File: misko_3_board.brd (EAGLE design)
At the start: 96 x 162 mm, 179 parts, among them IC1 ATMEGA1281-16AU, IC10 ORG1510-MK4, IC11 TPS3808G33DBVT, IC12 LTC4425, IC13 RN-42, IC14 ADXL345, IC15 74HCT1G32, IC16 FM25W256-SOIC, IC17 MICROSD_SPI_MODE, IC18 FH12-30S-0.5SH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

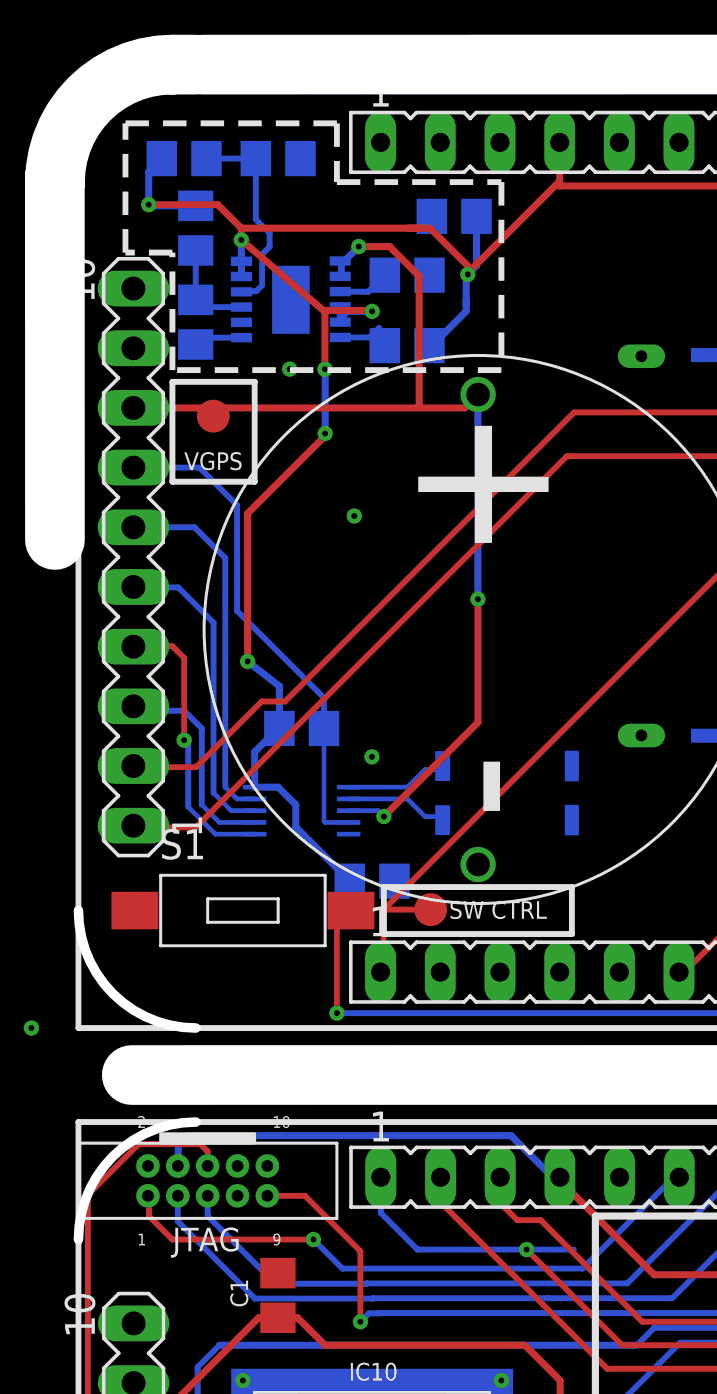
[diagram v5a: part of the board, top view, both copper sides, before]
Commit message: - corrected resisitor divider for LTC4425 - R60/61 now connect to Vgps (instead of Vcc)
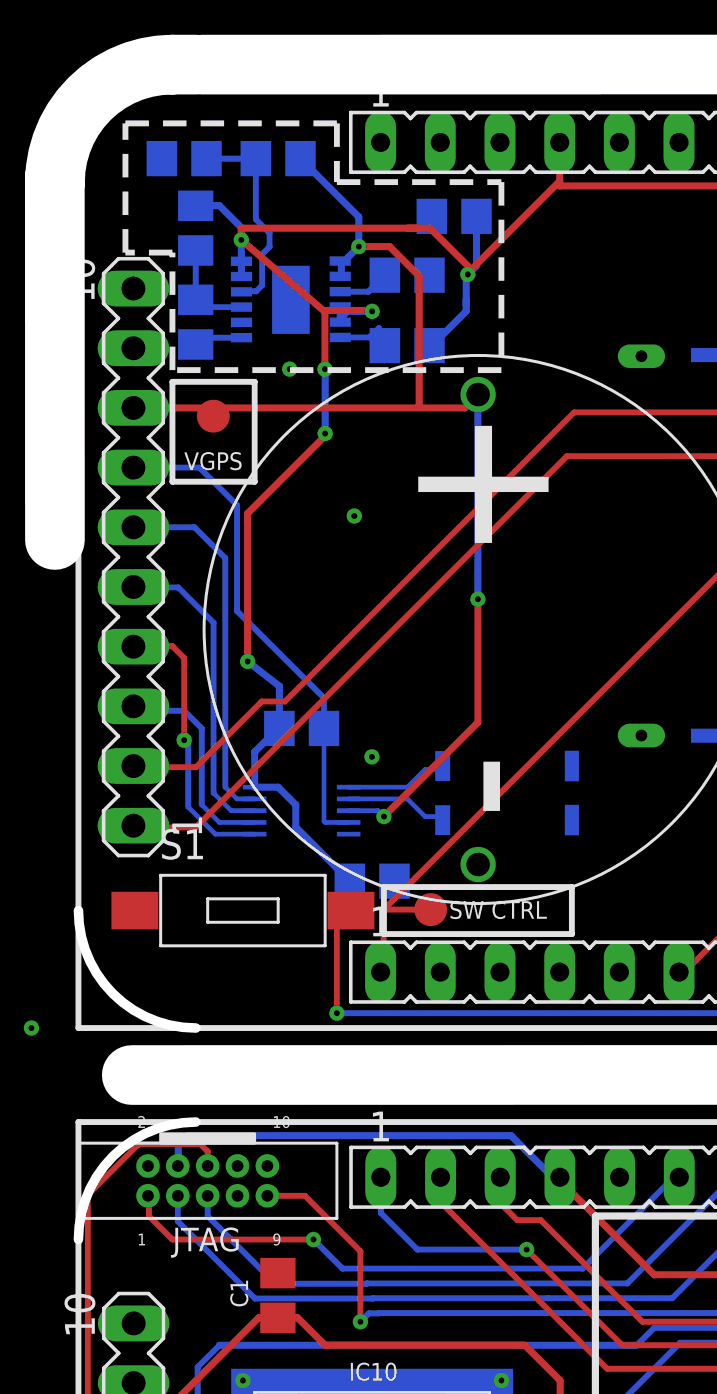
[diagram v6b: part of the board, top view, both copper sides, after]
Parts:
- moved R60 4.00 mm to (8.50, 125.0), turned to 180 degrees
- moved R61 4.00 mm to (4.50, 125.0), turned to 180 degrees
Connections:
- net VCC: no longer R60.2
- net VGPS: now also R60.2
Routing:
- net VCC: track 459.8 -> 454.1 mm, vias 34 -> 33
- net VGPS: track 107.3 -> 112.0 mm
- net RXD: track 64.5 -> 62.5 mm
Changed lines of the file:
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@@
 <setting verticaltext="up"/>
 </settings>
-<grid distance="1" unitdist="mm" unit="mm" style="lines" multiple="1" display="yes" altdistance="0.005" altunitdist="mm" altunit="mm"/>
+<grid distance="0.5" unitdist="mm" unit="mm" style="lines" multiple="1" display="yes" altdistance="0.005" altunitdist="mm" altunit="mm"/>
 <layers>
 <layer number="1" name="Top" color="4" fill="1" visible="yes" active="yes"/>
@@
 <attribute name="SPICETYPE" value="diode" x="97" y="10" size="1.778" layer="27" rot="R180" display="off"/>
 </element>
-<element name="R60" library="resistor" package="R0805" value="470k" x="4.5" y="125" rot="MR0"/>
-<element name="R61" library="resistor" package="R0805" value="470k" x="8.5" y="125" rot="MR0"/>
+<element name="R60" library="resistor" package="R0805" value="470k" x="8.5" y="125" rot="MR180"/>
+<element name="R61" library="resistor" package="R0805" value="470k" x="4.5" y="125" rot="MR180"/>
 <element name="S1" library="DTSM-32N-B" package="DTSM-32N-B" value="" x="7" y="93">
 <attribute name="MF" value="" x="7" y="93" size="1.778" layer="27" display="off"/>
@@
 <via x="34.2212" y="10.74" extent="1-16" drill="0.7" shape="octagon"/>
 <contactref element="IC20" pad="VCC"/>
-<wire x1="5.04" y1="123.04" x2="4.99" y2="122.99" width="0.3" layer="16"/>
+<wire x1="4.99" y1="122.99" x2="5.04" y2="123.04" width="0.3" layer="16"/>
 <wire x1="16.57" y1="120.07" x2="16.54" y2="120.04" width="0.3" layer="16"/>
 <via x="16.57" y="120.07" extent="1-16" drill="0.25"/>
@@
 <wire x1="34.99" y1="107.3354" x2="34.99" y2="106.64520625" width="0.3" layer="1"/>
 <wire x1="34.99" y1="106.64520625" x2="34.53919375" y2="106.1944" width="0.3" layer="1"/>
-<wire x1="4.99" y1="122.99" x2="3.04" y2="122.99" width="0.3" layer="16"/>
-<wire x1="3.04" y1="122.99" x2="2.99" y2="123.04" width="0.3" layer="16"/>
-<via x="2.99" y="123.04" extent="1-16" drill="0.25"/>
-<wire x1="5.9308" y1="123.04" x2="2.99" y2="123.04" width="0.3" layer="1"/>
 <via x="6.9308" y="121.54" extent="1-16" drill="0.25"/>
 <wire x1="10.49" y1="116.04" x2="10.39" y2="116.14" width="0.3" layer="16"/>
@@
 <wire x1="67.25" y1="50.25" x2="72.584" y2="55.584" width="0.3" layer="1"/>
 <wire x1="6.94" y1="120.63" x2="6.94" y2="120.94" width="0.3" layer="16"/>
-<wire x1="6.9308" y1="121.54" x2="6.9308" y2="120.6392" width="0.3" layer="16"/>
+<wire x1="6.9308" y1="120.6392" x2="6.9308" y2="121.54" width="0.3" layer="16"/>
 <wire x1="6.9308" y1="120.6392" x2="6.94" y2="120.63" width="0.3" layer="16"/>
 <wire x1="6.9308" y1="121.54" x2="6.9308" y2="122.04" width="0.3" layer="1"/>
-<wire x1="6.9308" y1="122.04" x2="5.9308" y2="123.04" width="0.3" layer="1"/>
 <wire x1="14.96" y1="122.04" x2="6.9308" y2="122.04" width="0.3" layer="1"/>
 <wire x1="14" y1="122.04" x2="14.46" y2="122.04" width="0.3" layer="1"/>
@@
 <wire x1="12.5" y1="118.5" x2="11.33" y2="118.5" width="0.3" layer="16"/>
 <wire x1="11.33" y1="118.5" x2="11.14" y2="118.69" width="0.3" layer="16"/>
-<contactref element="R60" pad="2"/>
-<wire x1="2.99" y1="123.04" x2="2.99" y2="124.44" width="0.3" layer="16"/>
-<wire x1="2.99" y1="124.44" x2="3.55" y2="125" width="0.3" layer="16"/>
+<wire x1="6.9308" y1="121.54" x2="6.9308" y2="122.0692" width="0.3" layer="16"/>
+<wire x1="6.9308" y1="122.0692" x2="6" y2="123" width="0.3" layer="16"/>
+<wire x1="6" y1="123" x2="5" y2="123" width="0.3" layer="16"/>
+<wire x1="5" y1="123" x2="4.99" y2="122.99" width="0.3" layer="16"/>
 <wire x1="20.48" y1="125.69" x2="15.37" y2="145" width="0" layer="19" extent="1-1"/>
 <wire x1="16.5" y1="119" x2="16.5" y2="118.75" width="0" layer="19" extent="16-16"/>
@@
 <wire x1="13.245" y1="121.255" x2="14.5" y2="120" width="0.3" layer="1"/>
 <wire x1="14.5" y1="120" x2="14.5" y2="114.5" width="0.3" layer="1"/>
+<contactref element="R60" pad="2"/>
+<wire x1="11.9308" y1="121.255" x2="11.9308" y2="122.5192" width="0.3" layer="16"/>
+<wire x1="11.9308" y1="122.5192" x2="9.45" y2="125" width="0.3" layer="16"/>
 <wire x1="16.44" y1="114.39" x2="14.5" y2="114.5" width="0" layer="19" extent="1-1"/>
 <wire x1="17" y1="115.03" x2="17.01" y2="114.96" width="0" layer="19" extent="16-16"/>
@@
 <contactref element="R60" pad="1"/>
 <contactref element="R61" pad="2"/>
+<wire x1="7.55" y1="122.415275" x2="8.134" y2="121.831275" width="0.25" layer="16"/>
 <wire x1="5.45" y1="125" x2="7.55" y2="125" width="0.25" layer="16"/>
 <wire x1="7.55" y1="125" x2="7.55" y2="122.415275" width="0.25" layer="16"/>
-<wire x1="7.55" y1="122.415275" x2="8.134" y2="121.831275" width="0.25" layer="16"/>
 </signal>
 <signal name="PFI_RET" class="2">
@@
 <wire x1="12.87" y1="81.65" x2="12.87" y2="80.13" width="0.25" layer="16"/>
 <wire x1="23.1443875" y1="74.5" x2="19.07219375" y2="78.57219375" width="0.25" layer="1"/>
-<wire x1="21.07" y1="78.56" x2="21.07" y2="78.57" width="0.25" layer="16"/>
-<wire x1="21.07" y1="78.57" x2="19.07219375" y2="78.57219375" width="0.25" layer="16"/>
 <via x="19.07219375" y="78.57219375" extent="1-16" drill="0.25"/>
 <wire x1="19.07219375" y1="78.57219375" x2="14.42780625" y2="78.57219375" width="0.25" layer="16"/>

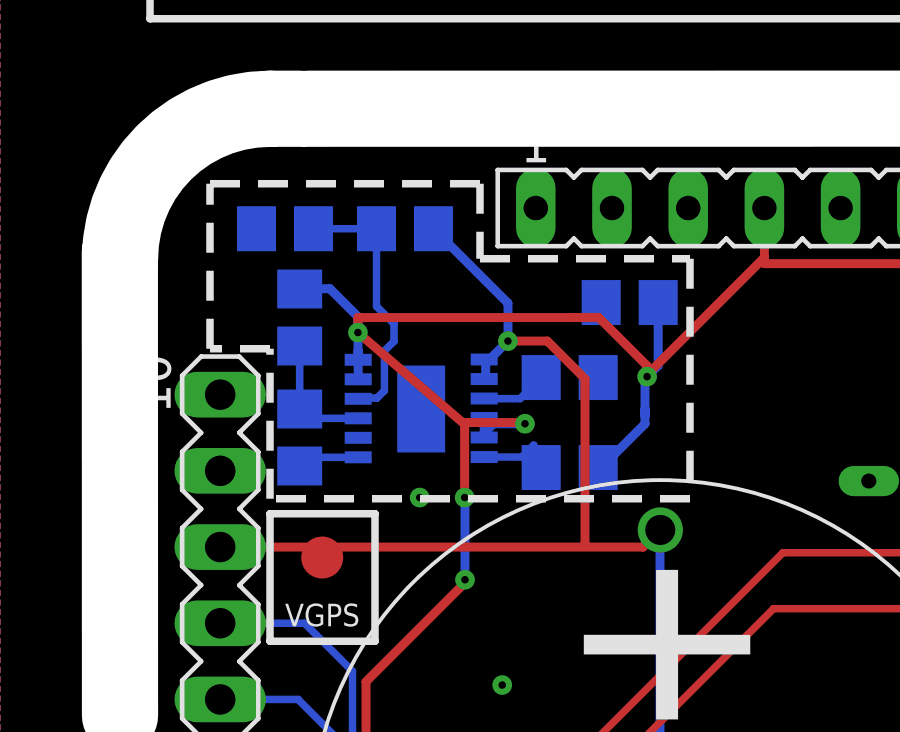
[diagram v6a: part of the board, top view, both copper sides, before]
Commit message: - removed power fail functionality from LTC4425 since it is not needed at all
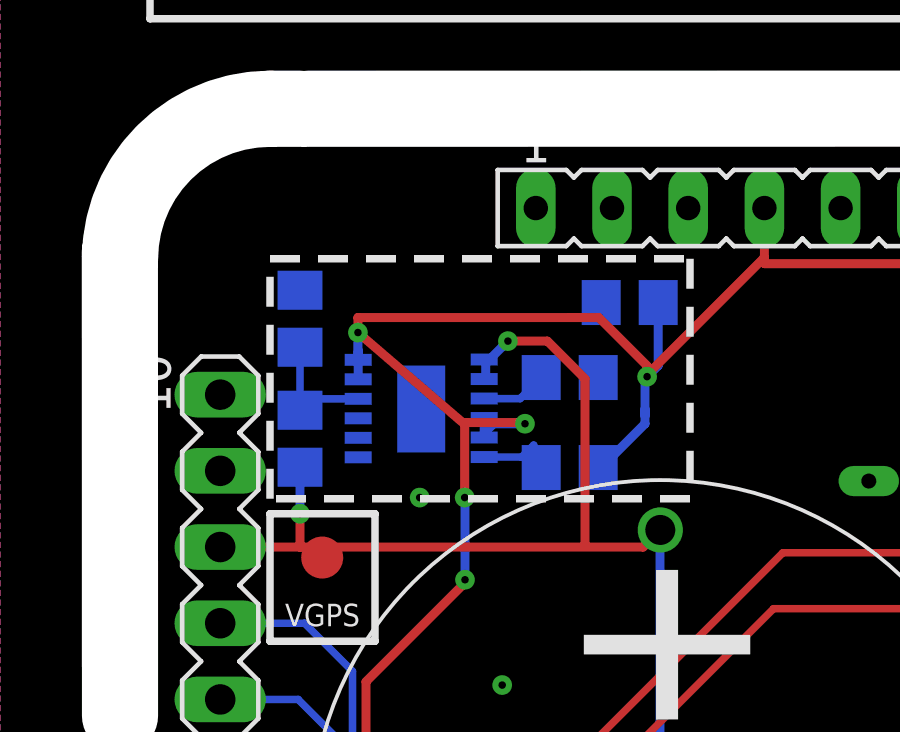
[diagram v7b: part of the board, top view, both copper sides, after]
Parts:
- removed R37, R38: 150k, resistor:R0805
- moved R60 7.83 mm to (5.00, 118.0), turned to 270 degrees
- moved R61 3.04 mm to (5.00, 122.0), turned to 270 degrees
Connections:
- removed net PFI: IC12.PFI, R37.2, R38.1
- net PFI_RET: no longer R37.1
- net VCC: no longer R38.2
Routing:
- net VMID: track 9.00 -> 4.33 mm
- net PFI: track 4.18 -> 0.00 mm
- net VCC: track 454.1 -> 451.2 mm
- net VGPS: track 112.0 -> 109.9 mm, vias 5 -> 6
- net PFI_RET: track 2.07 -> 0.00 mm
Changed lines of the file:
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@@
 <wire x1="18" y1="124" x2="18" y2="116" width="0.25" layer="21" style="shortdash"/>
 <wire x1="18" y1="116" x2="4" y2="116" width="0.25" layer="21" style="shortdash"/>
-<wire x1="4" y1="116" x2="4" y2="121" width="0.25" layer="21" style="shortdash"/>
-<wire x1="4" y1="121" x2="2" y2="121" width="0.25" layer="21" style="shortdash"/>
-<wire x1="2" y1="121" x2="2" y2="126.5" width="0.25" layer="21" style="shortdash"/>
-<wire x1="2" y1="126.5" x2="11" y2="126.5" width="0.25" layer="21" style="shortdash"/>
-<wire x1="11" y1="126.5" x2="11" y2="124" width="0.25" layer="21" style="shortdash"/>
-<wire x1="11" y1="124" x2="18" y2="124" width="0.25" layer="21" style="shortdash"/>
-<wire x1="17.99" y1="124.04" x2="10.99" y2="124.04" width="0.25" layer="22" style="shortdash"/>
-<wire x1="10.99" y1="124.04" x2="10.99" y2="126.54" width="0.254" layer="22" style="shortdash"/>
-<wire x1="10.99" y1="126.54" x2="1.99" y2="126.54" width="0.25" layer="22" style="shortdash"/>
-<wire x1="1.99" y1="126.54" x2="1.99" y2="121.04" width="0.25" layer="22" style="shortdash"/>
-<wire x1="1.99" y1="121.04" x2="3.99" y2="121.04" width="0.25" layer="22" style="shortdash"/>
-<wire x1="3.99" y1="121.04" x2="3.99" y2="116.04" width="0.25" layer="22" style="shortdash"/>
+<wire x1="4" y1="116" x2="4" y2="124" width="0.25" layer="21" style="shortdash"/>
+<wire x1="4" y1="124" x2="18" y2="124" width="0.25" layer="21" style="shortdash"/>
+<wire x1="17.99" y1="124.04" x2="3.99" y2="124.04" width="0.25" layer="22" style="shortdash"/>
+<wire x1="3.99" y1="124.04" x2="3.99" y2="116.04" width="0.25" layer="22" style="shortdash"/>
 <wire x1="3.99" y1="116.04" x2="17.99" y2="116.04" width="0.25" layer="22" style="shortdash"/>
 <wire x1="17.99" y1="116.04" x2="17.99" y2="124.04" width="0.25" layer="22" style="shortdash"/>
@@
 <attribute name="VALUE" x="21.865" y="67.54" size="1.27" layer="28" rot="MR180"/>
 </element>
-<element name="R37" library="resistor" package="R0805" value="150k" x="4.99" y="118.04" smashed="yes" rot="MR90">
-<attribute name="NAME" x="6.25" y="117" size="0.75" layer="26" rot="MR90"/>
-<attribute name="VALUE" x="2.45" y="117.405" size="1.27" layer="28" rot="MR90"/>
-</element>
-<element name="R38" library="resistor" package="R0805" value="150k" x="4.99" y="122.04" smashed="yes" rot="MR90">
-<attribute name="NAME" x="6.25" y="121.25" size="0.75" layer="26" rot="MR90"/>
-<attribute name="VALUE" x="2.45" y="121.405" size="1.27" layer="28" rot="MR90"/>
-</element>
 <element name="R39" library="resistor" package="R0805" value="1k" x="13.99" y="117.04" smashed="yes" rot="MR0">
 <attribute name="NAME" x="17.75" y="116.5" size="0.75" layer="26" rot="MR0"/>
@@
 <attribute name="SPICETYPE" value="diode" x="97" y="10" size="1.778" layer="27" rot="R180" display="off"/>
 </element>
-<element name="R60" library="resistor" package="R0805" value="470k" x="8.5" y="125" rot="MR180"/>
-<element name="R61" library="resistor" package="R0805" value="470k" x="4.5" y="125" rot="MR180"/>
+<element name="R60" library="resistor" package="R0805" value="470k" x="5" y="118" rot="MR270"/>
+<element name="R61" library="resistor" package="R0805" value="470k" x="5" y="122" rot="MR270"/>
 <element name="S1" library="DTSM-32N-B" package="DTSM-32N-B" value="" x="7" y="93">
 <attribute name="MF" value="" x="7" y="93" size="1.778" layer="27" display="off"/>
@@
 <contactref element="IC12" pad="FB"/>
 <contactref element="IC12" pad="SEL"/>
-<contactref element="R38" pad="2"/>
 <contactref element="IC12" pad="VIN1"/>
 <contactref element="C21" pad="2"/>
@@
 <via x="34.2212" y="10.74" extent="1-16" drill="0.7" shape="octagon"/>
 <contactref element="IC20" pad="VCC"/>
-<wire x1="4.99" y1="122.99" x2="5.04" y2="123.04" width="0.3" layer="16"/>
 <wire x1="16.57" y1="120.07" x2="16.54" y2="120.04" width="0.3" layer="16"/>
 <via x="16.57" y="120.07" extent="1-16" drill="0.25"/>
@@
 <wire x1="12.5" y1="118.5" x2="11.33" y2="118.5" width="0.3" layer="16"/>
 <wire x1="11.33" y1="118.5" x2="11.14" y2="118.69" width="0.3" layer="16"/>
-<wire x1="6.9308" y1="121.54" x2="6.9308" y2="122.0692" width="0.3" layer="16"/>
-<wire x1="6.9308" y1="122.0692" x2="6" y2="123" width="0.3" layer="16"/>
-<wire x1="6" y1="123" x2="5" y2="123" width="0.3" layer="16"/>
-<wire x1="5" y1="123" x2="4.99" y2="122.99" width="0.3" layer="16"/>
 <wire x1="20.48" y1="125.69" x2="15.37" y2="145" width="0" layer="19" extent="1-1"/>
 <wire x1="16.5" y1="119" x2="16.5" y2="118.75" width="0" layer="19" extent="16-16"/>
@@
 <wire x1="5" y1="28" x2="6.05" y2="28" width="0.3048" layer="1"/>
 <wire x1="5.49" y1="114.39" x2="16.44" y2="114.39" width="0.3" layer="1"/>
-<wire x1="5.49" y1="114.39" x2="2.34" y2="114.39" width="0.3" layer="1"/>
+<wire x1="5.49" y1="114.39" x2="5" y2="114.39" width="0.3" layer="1"/>
 <contactref element="TP10" pad="TP"/>
+<wire x1="5" y1="114.39" x2="2.34" y2="114.39" width="0.3" layer="1"/>
 <wire x1="5.74" y1="114.04" x2="5.49" y2="114.39" width="0.3" layer="1"/>
 <contactref element="TP11" pad="TP"/>
@@
 <wire x1="14.5" y1="120" x2="14.5" y2="114.5" width="0.3" layer="1"/>
 <contactref element="R60" pad="2"/>
-<wire x1="11.9308" y1="121.255" x2="11.9308" y2="122.5192" width="0.3" layer="16"/>
-<wire x1="11.9308" y1="122.5192" x2="9.45" y2="125" width="0.3" layer="16"/>
+<wire x1="11.9308" y1="121.255" x2="11.9308" y2="122.5192" width="0" layer="19" extent="1-16"/>
+<wire x1="5" y1="114.39" x2="5" y2="115.5" width="0.3" layer="1"/>
+<via x="5" y="115.5" extent="1-16" drill="0.25"/>
+<wire x1="5" y1="115.5" x2="5" y2="117.05" width="0.3" layer="16"/>
 <wire x1="16.44" y1="114.39" x2="14.5" y2="114.5" width="0" layer="19" extent="1-1"/>
 <wire x1="17" y1="115.03" x2="17.01" y2="114.96" width="0" layer="19" extent="16-16"/>
@@
 <wire x1="6.05" y1="28" x2="14.5" y2="55" width="0" layer="19" extent="1-1"/>
 </signal>
-<signal name="PFI" class="2">
-<contactref element="R37" pad="2"/>
-<contactref element="R38" pad="1"/>
-<contactref element="IC12" pad="PFI"/>
-<wire x1="4.99" y1="118.99" x2="4.99" y2="121.09" width="0.254" layer="16"/>
-<wire x1="6.94" y1="118.68" x2="5.3" y2="118.68" width="0.25" layer="16"/>
-<wire x1="5.3" y1="118.68" x2="4.99" y2="118.99" width="0.25" layer="16"/>
-</signal>
 <signal name="LTC4425_PROG" class="2">
 <contactref element="R40" pad="2"/>
@@
 <contactref element="IC12" pad="VMID"/>
 <wire x1="6.80841875" y1="119.29" x2="6.94" y2="119.33" width="0.254" layer="16"/>
-<wire x1="7.56604375" y1="119.355" x2="7.815" y2="119.60395625" width="0.25" layer="16"/>
-<wire x1="7.815" y1="120.929725" x2="8.134" y2="121.248725" width="0.25" layer="16"/>
-<wire x1="8.134" y1="121.831275" x2="8.134" y2="121.248725" width="0.25" layer="16"/>
-<wire x1="7.815" y1="119.60395625" x2="7.815" y2="120.929725" width="0.25" layer="16"/>
-<wire x1="6.94" y1="119.33" x2="6.965" y2="119.355" width="0.25" layer="16"/>
-<wire x1="6.965" y1="119.355" x2="7.56604375" y2="119.355" width="0.25" layer="16"/>
 <contactref element="R60" pad="1"/>
 <contactref element="R61" pad="2"/>
-<wire x1="7.55" y1="122.415275" x2="8.134" y2="121.831275" width="0.25" layer="16"/>
-<wire x1="5.45" y1="125" x2="7.55" y2="125" width="0.25" layer="16"/>
-<wire x1="7.55" y1="125" x2="7.55" y2="122.415275" width="0.25" layer="16"/>
-</signal>
-<signal name="PFI_RET" class="2">
-<contactref element="R37" pad="1"/>
-<contactref element="IC12" pad="PFI_RET"/>
-<wire x1="6.94" y1="117.38" x2="5.28" y2="117.38" width="0.25" layer="16"/>
-<wire x1="5.28" y1="117.38" x2="4.99" y2="117.09" width="0.25" layer="16"/>
+<wire x1="5" y1="118.95" x2="5" y2="121.05" width="0.25" layer="16"/>
+<wire x1="6.94" y1="119.33" x2="5.38" y2="119.33" width="0.25" layer="16"/>
+<wire x1="5.38" y1="119.33" x2="5" y2="118.95" width="0.25" layer="16"/>
 </signal>
 <signal name="GPIO7" class="2">
@@
 <wire x1="103.35" y1="10" x2="99" y2="22.57" width="0" layer="19" extent="1-1"/>
 </signal>
+<signal name="PFI_RET" class="2">
+<contactref element="IC12" pad="PFI_RET"/>
+</signal>
 </signals>
